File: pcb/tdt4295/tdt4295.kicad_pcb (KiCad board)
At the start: 6 copper layers, 209.6 x 139.7 mm, 170 parts, among them J101 ARM 20 Pin Debug Header, J102 MCU USART1 Header, J103 DM1AA-SF-PEJ(21), J104 MCU GPIO Header, J301 FPGA__debug, J501 618015330923, J502 FPGA GPIO, P201 690-005-299-043, U101 EFM32GG12B810F1024GQ64, U102 COM-09032 Joystick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

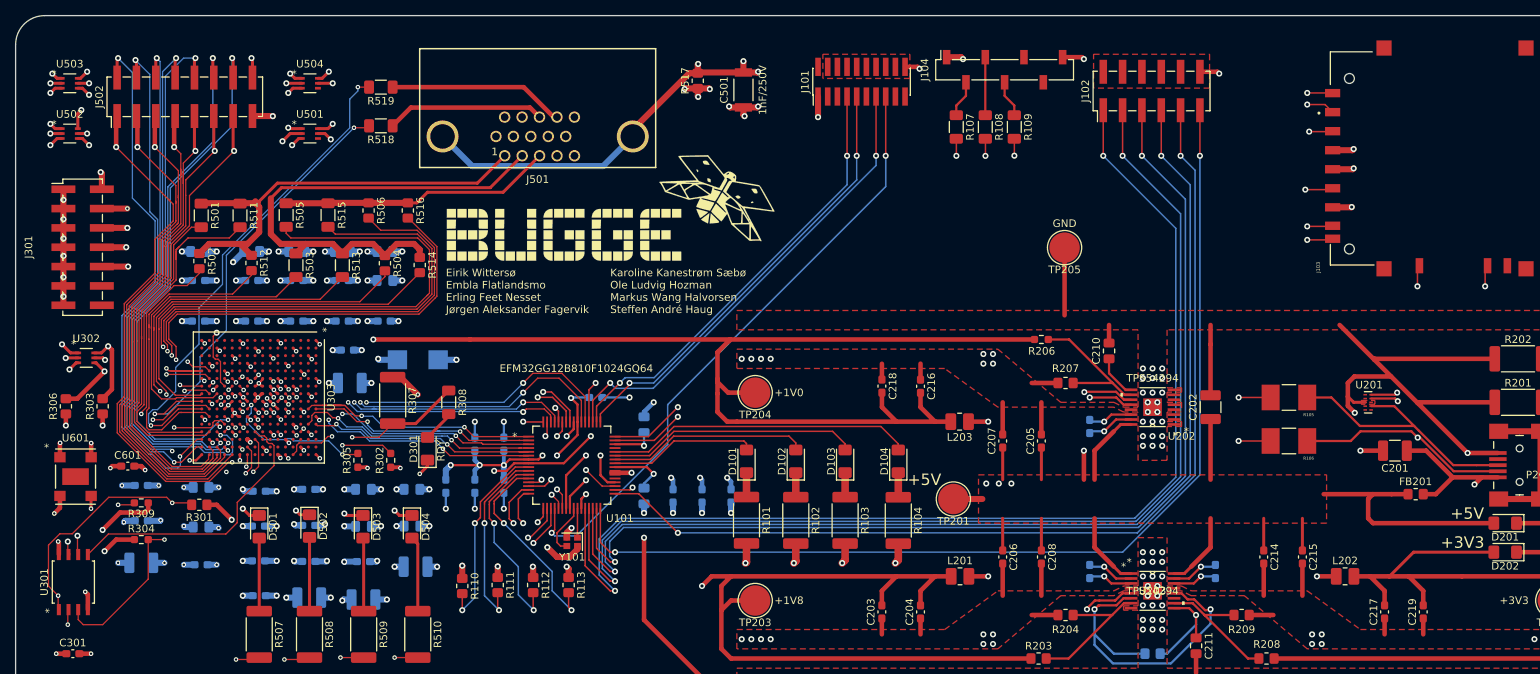
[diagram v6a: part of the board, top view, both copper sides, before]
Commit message: touch up the silkscreen
header annotations etc.
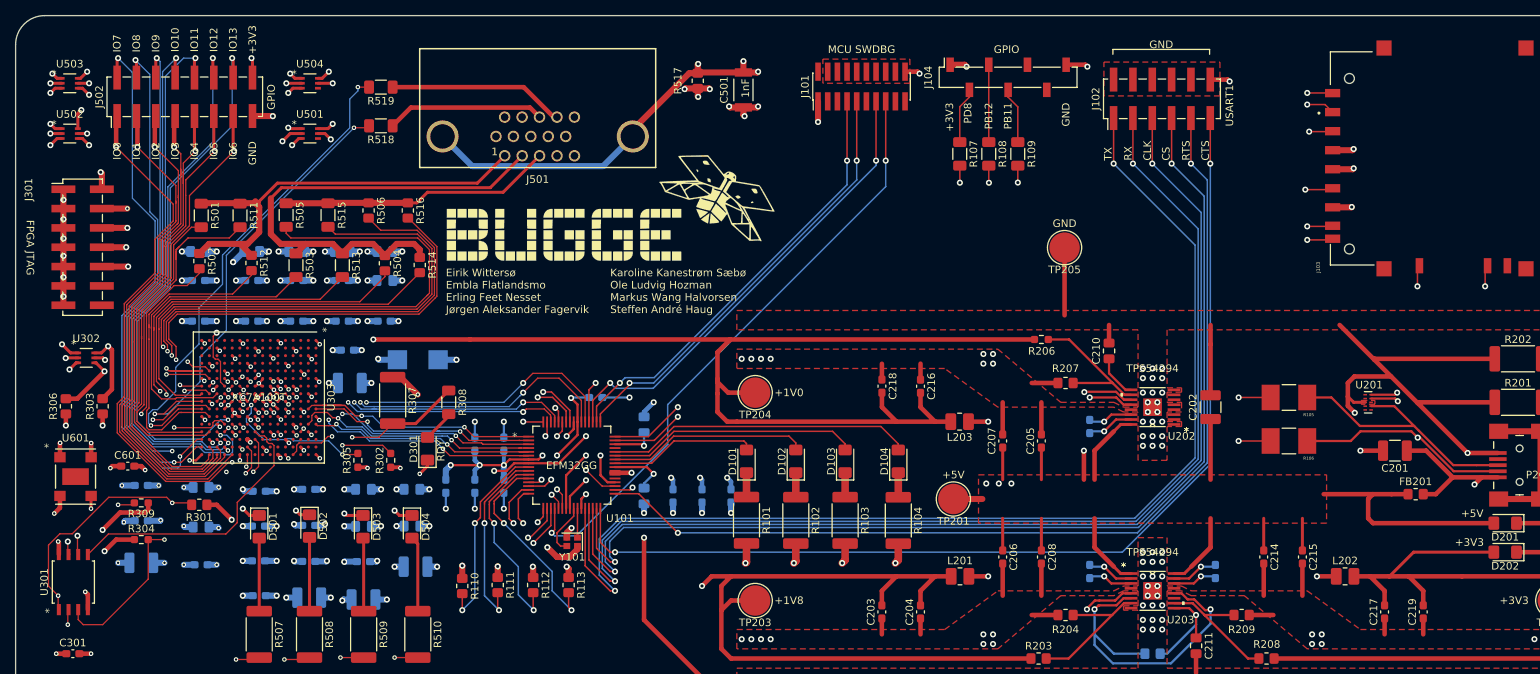
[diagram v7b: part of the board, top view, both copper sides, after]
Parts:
- C501: value 1nF/250V -> 1nF
- U101: value EFM32GG12B810F1024GQ64 -> EFM32GG
- moved R109 3.56 mm to (184.4, 41.7)
- moved R107 3.56 mm to (176.7, 41.7)
- moved R108 3.56 mm to (180.5, 41.7)
- moved J102 1.70 mm to (203.3, 34.4)
- moved J104 1.09 mm to (183.1, 31.6)
- moved J101 0.63 mm to (163.8, 32.8)
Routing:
- net Net-(J104-Pad4): track 4.85 -> 7.39 mm
- net Net-(J104-Pad2): track 4.85 -> 7.39 mm
- net Net-(J104-Pad3): track 7.62 -> 10.2 mm
- net GND: track 481.0 -> 479.8 mm
- net +3V3: track 902.3 -> 903.5 mm
- net GPIO_PD8: track 74.2 -> 73.2 mm
- net GPIO_PB12: track 82.1 -> 81.1 mm
- net GPIO_PB11: track 87.7 -> 86.7 mm
- net MCU_RESETN: track 81.3 -> 80.7 mm
- net DBG_SWO: track 62.5 -> 61.8 mm
- net DBG_SWDIO: track 58.6 -> 58.0 mm
- net DBG_SWCLK: track 58.6 -> 57.9 mm
- net USART1_TX: track 151.8 -> 152.3 mm
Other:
- board text added: "CLK"
- board text added: "CS"
- board text added: "CTS"
- board text added: "FPGA JTAG"
- board text added: "GPIO"
- board text added: "IO0"
- board text added: "IO1"
- board text added: "IO10"
- board text added: "IO11"
- board text added: "IO12"
- board text added: "IO13"
- board text added: "IO2"
- board text added: "IO3"
- board text added: "IO4"
- board text added: "IO5"
- board text added: "IO6"
- board text added: "IO7"
- board text added: "IO8"
- board text added: "IO9"
- board text added: "MCU SWDBG"
- board text added: "PB11"
- board text added: "PB12"
- board text added: "PD8"
- board text added: "RTS"
- board text added: "RX"
- board text added: "TX"
- board text added: "USART1"
- board text added: "XC7A100T"

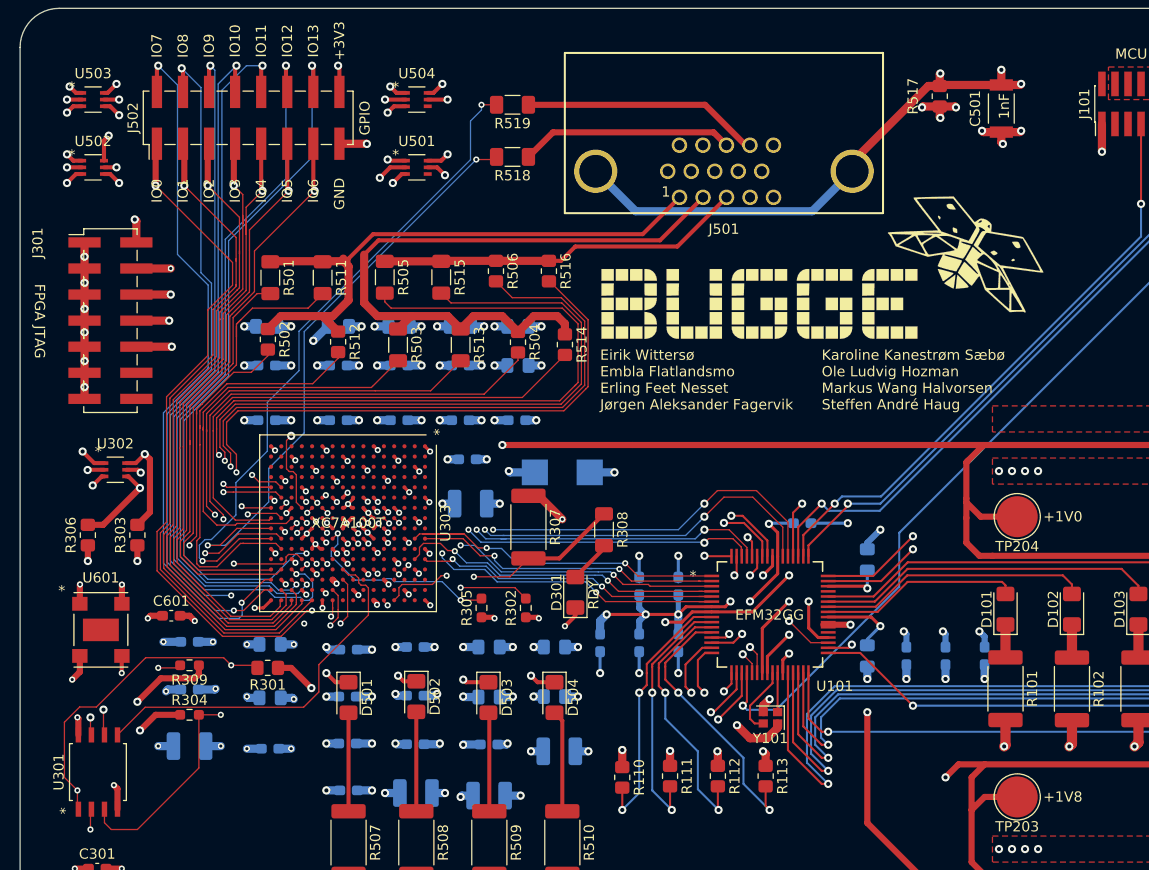
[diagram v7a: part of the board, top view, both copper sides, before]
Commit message: more routing jank fixes
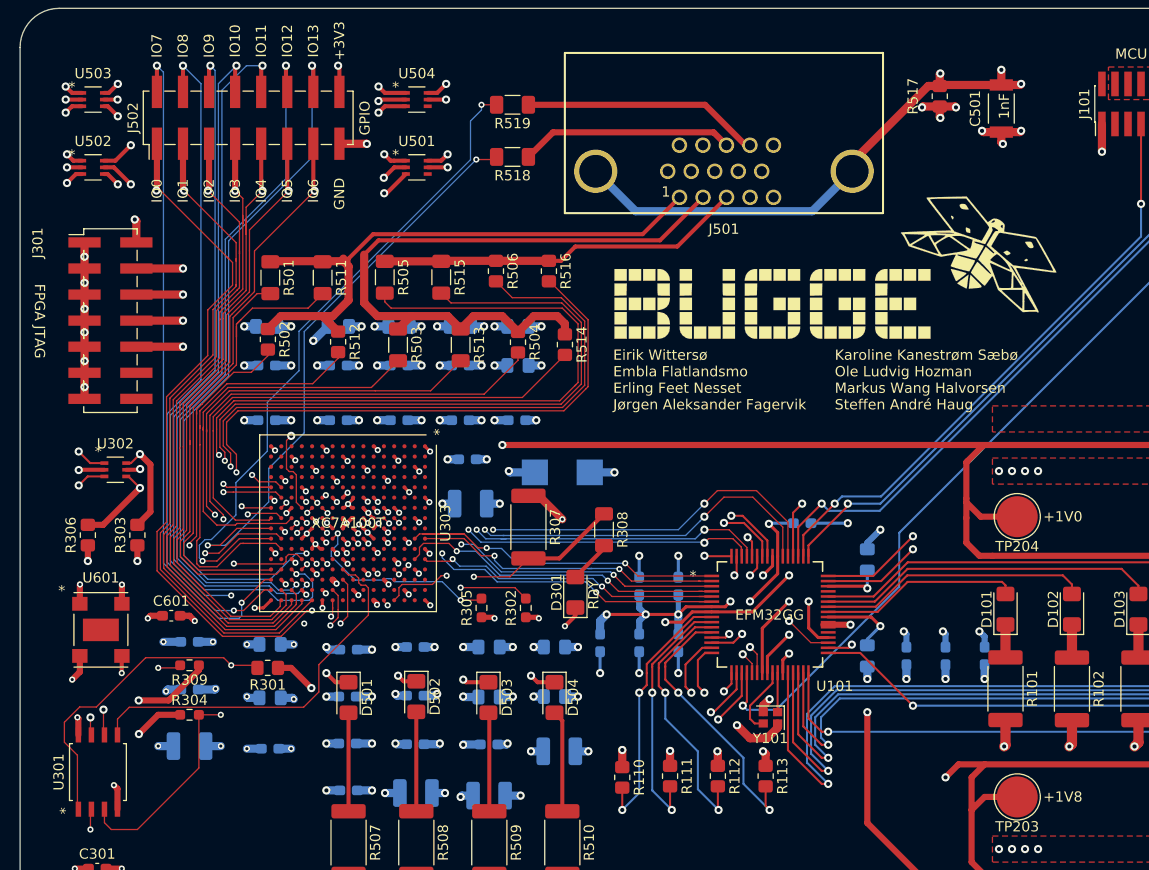
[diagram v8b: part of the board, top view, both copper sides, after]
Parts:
- moved G*** 1.27 mm to (132.1, 48.9)
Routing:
- net /FPGA/TDI_JTAG: track 61.1 -> 53.5 mm
- net /FPGA/TCK_JTAG: track 71.5 -> 64.6 mm
- net FPGA_EXT_IO7: track 81.0 -> 77.9 mm
- net FPGA_EXT_IO1: track 77.9 -> 75.8 mm
- net FPGA_EXT_IO0: track 86.6 -> 84.7 mm
- net +3V3: track 903.5 -> 905.3 mm
- net FPGA_EXT_IO13: track 84.6 -> 85.9 mm
- net /FPGA/TMS_JTAG: track 69.6 -> 68.4 mm
- net /FPGA/TDO_JTAG: track 67.2 -> 68.3 mm
- net /FPGA/IOB14/QSPI_DQ0: track 37.0 -> 37.9 mm
- net FPGA_EXT_IO12: track 86.0 -> 86.7 mm
- net FPGA_EXT_IO4: track 76.6 -> 77.2 mm
- net FPGA_EXT_IO10: track 93.6 -> 94.2 mm
- net /FPGA/IOB14/QSPI_CS: vias 3 -> 2
